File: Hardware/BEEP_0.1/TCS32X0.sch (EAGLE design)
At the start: 12 parts, among them IC1 TCS32X0

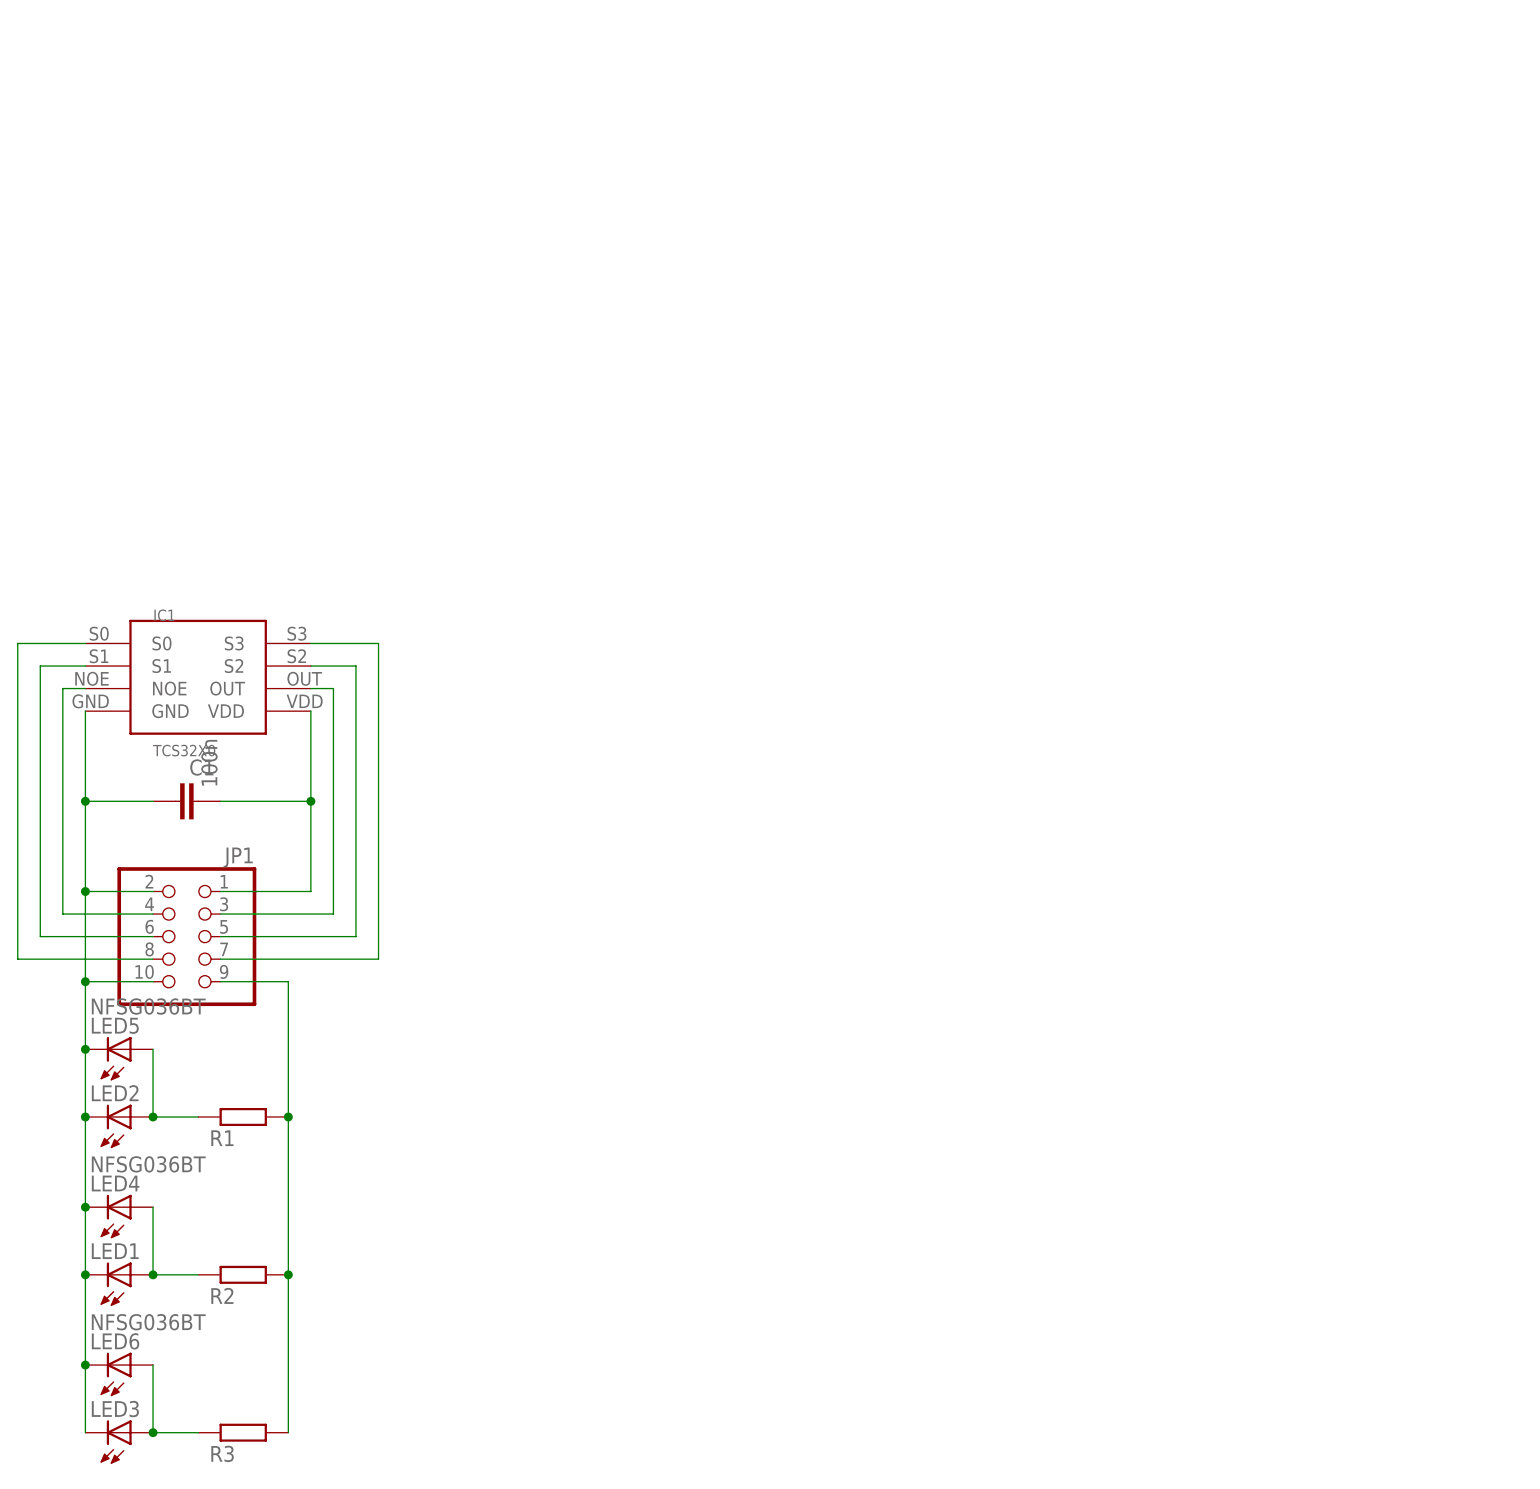
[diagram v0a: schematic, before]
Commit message: Add branding ;) enhance PCBs finish Easy RGB Board add Texas Instruments libray from Element 14 add dxf import ulp for eagle add Script for easy eagle export to pdf for etching minor cleanup
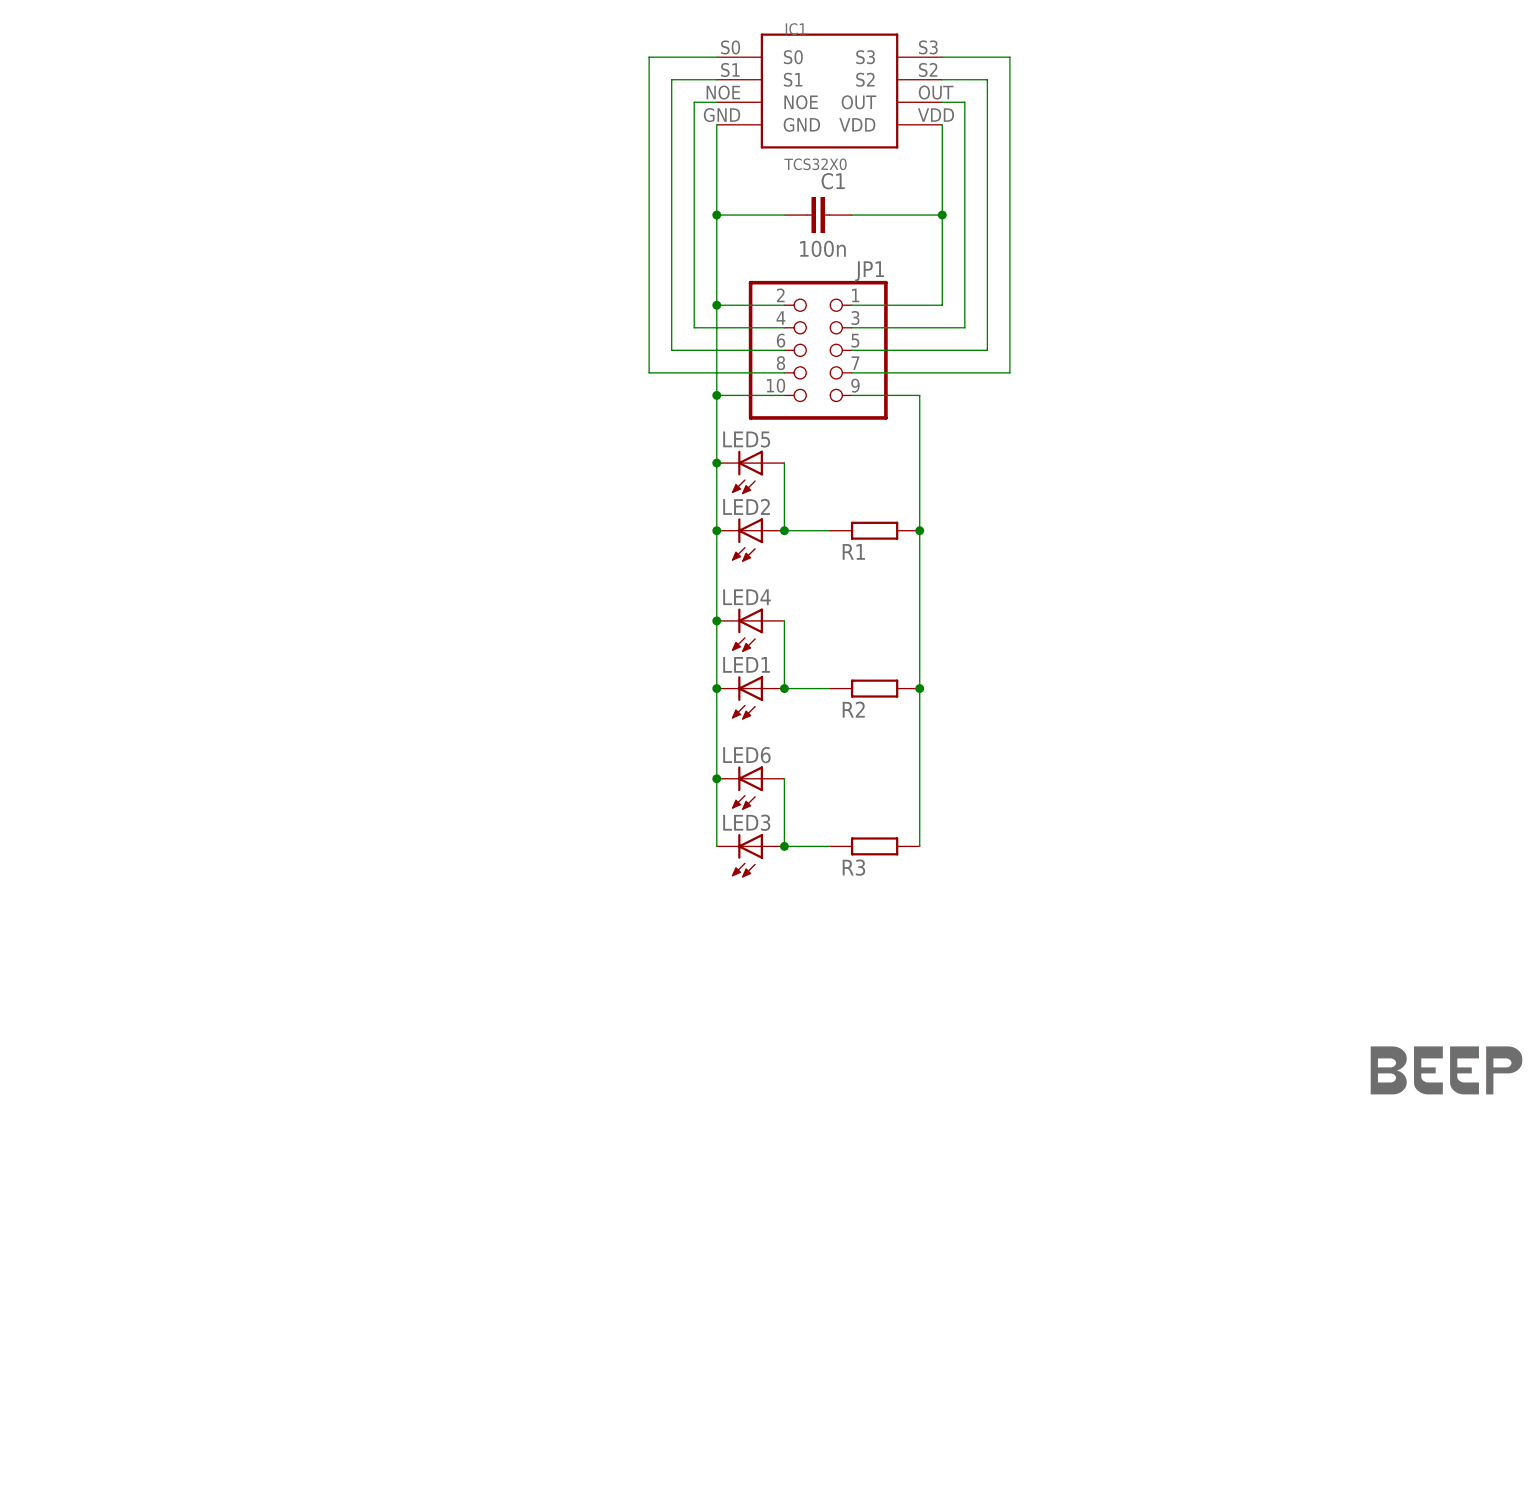
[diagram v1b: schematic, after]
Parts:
- added U$1: LOGO-COPPER4, Branding:LOGO-COPPER4
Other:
- moved on the sheet: C1, IC1, JP1, LED1, LED2, LED3, LED4, LED5, LED6, R1, R2, R3
